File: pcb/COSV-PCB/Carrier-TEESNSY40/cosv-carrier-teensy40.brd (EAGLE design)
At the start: 96.8 x 26.7 mm, 21 parts, among them K1 61200821621, K2 61200821621, K3 61200821621

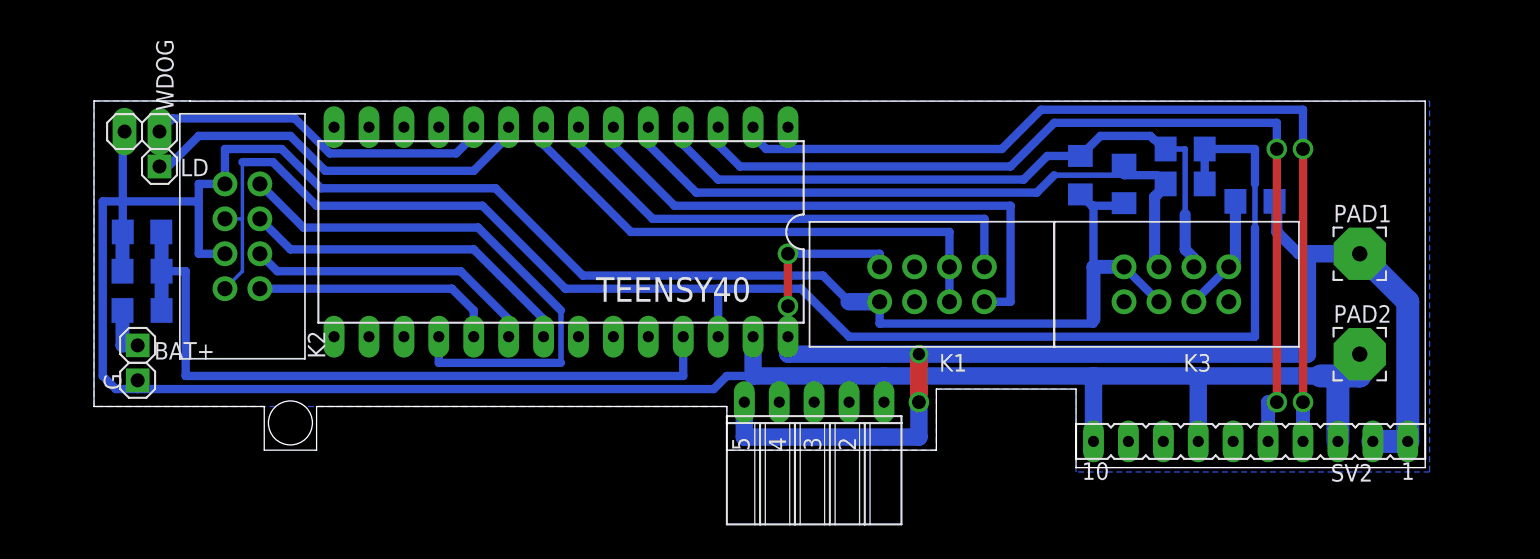
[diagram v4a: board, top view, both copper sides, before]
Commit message: Clean up part/pin names on board
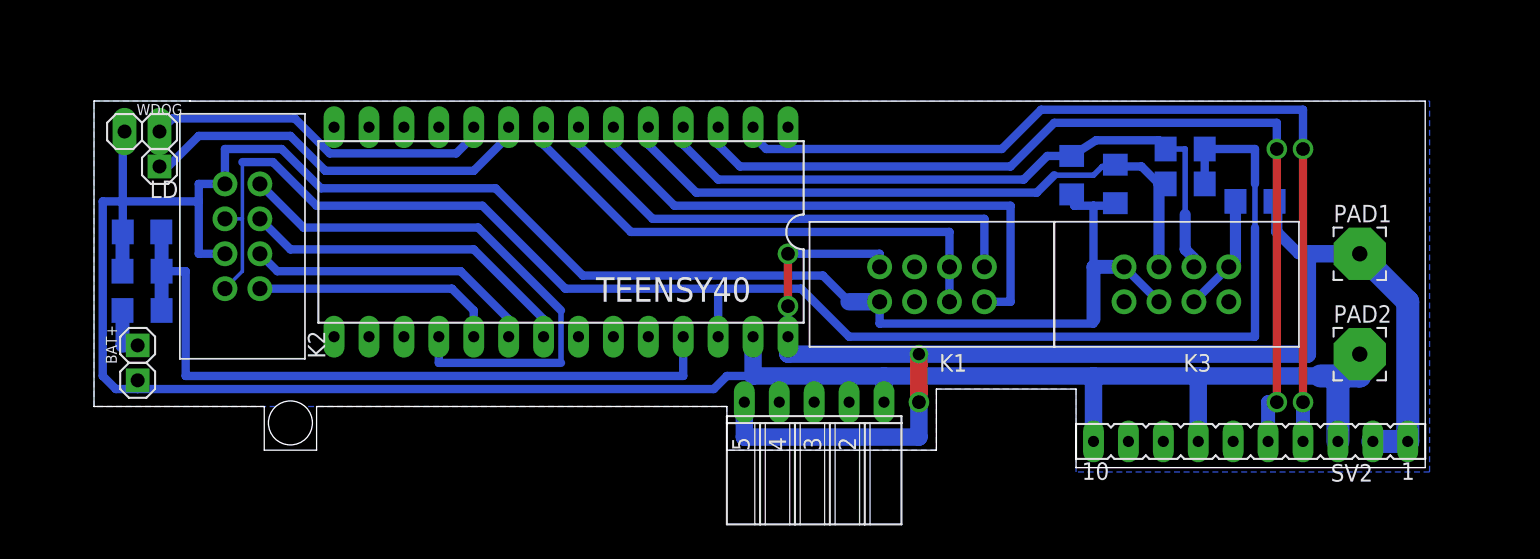
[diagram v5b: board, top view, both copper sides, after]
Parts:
- moved C2 0.64 mm to (74.6, 22.9)
- moved C3 0.64 mm to (77.8, 22.2)
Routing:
- net GND: track 242.4 -> 243.6 mm
- net ENCODER: track 48.4 -> 49.0 mm
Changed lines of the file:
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@@
 <?xml version="1.0" encoding="utf-8"?>
 <!DOCTYPE eagle SYSTEM "eagle.dtd">
-<eagle version="7.6.0">
+<eagle version="7.7.0">
 <drawing>
 <settings>
@@
 <text x="59.3725" y="16.8275" size="1.016" layer="27" rot="R180">vcc</text>
 <hole x="17.78" y="4.8387" drill="3.2"/>
+<text x="4.445" y="23.8125" size="1.016" layer="27">gnd</text>
+<text x="8.89" y="6.6675" size="1.016" layer="27" rot="R90">gnd</text>
 </plain>
 <attributes>
@@
 </element>
 <element name="BAT+" library="pinhead-2" package="1X01-S" value="" x="6.6675" y="10.4775" smashed="yes" rot="R270">
-<attribute name="NAME" x="7.8613" y="9.4488" size="1.27" layer="25" ratio="10"/>
+<attribute name="NAME" x="5.1562" y="9.1313" size="0.8128" layer="25" ratio="10" rot="R90"/>
 <attribute name="VALUE" x="3.4925" y="11.7475" size="1.27" layer="27" rot="R270"/>
 </element>
 <element name="GOLD_ORB_SM1" library="oshw" package="OSHW_8MM" value="OSHWLOGOLOGO8MM" x="27.305" y="19.05" rot="MR90"/>
 <element name="R3" library="resistor" package="R1206" value="2k2" x="82.8675" y="22.225" smashed="yes" rot="MR180">
-<attribute name="VALUE" x="86.36" y="23.495" size="1.27" layer="28" rot="MR270"/>
+<attribute name="VALUE" x="80.645" y="21.2725" size="1.27" layer="28" rot="MR180"/>
 </element>
 <element name="R4" library="resistor" package="R1206" value="2k2" x="82.8675" y="24.765" smashed="yes" rot="MR180">
-<attribute name="VALUE" x="86.36" y="26.035" size="1.27" layer="28" rot="MR270"/>
+<attribute name="VALUE" x="85.09" y="25.7175" size="1.27" layer="28" rot="MR0"/>
 </element>
 <element name="WDOG" library="pinhead" package="1X02" value="" x="6.985" y="26.035" smashed="yes">
-<attribute name="NAME" x="9.2837" y="27.5463" size="1.27" layer="25" ratio="10" rot="R90"/>
+<attribute name="NAME" x="6.5913" y="27.2288" size="0.8128" layer="25" ratio="10"/>
 <attribute name="VALUE" x="4.445" y="22.86" size="1.27" layer="27"/>
 </element>
 <element name="G" library="pinhead-2" package="1X01-S" value="" x="6.6675" y="7.9375" smashed="yes">
-<attribute name="NAME" x="5.4737" y="7.2263" size="1.27" layer="25" ratio="10" rot="R90"/>
 <attribute name="VALUE" x="5.3975" y="4.7625" size="1.27" layer="27"/>
 </element>
 <element name="LD" library="pinhead-2" package="1X01-S" value="" x="8.255" y="23.495" smashed="yes">
-<attribute name="NAME" x="9.7663" y="22.7838" size="1.27" layer="25" ratio="10"/>
+<attribute name="NAME" x="7.5438" y="21.1963" size="1.27" layer="25" ratio="10"/>
 <attribute name="VALUE" x="6.985" y="20.32" size="1.27" layer="27"/>
 </element>
-<element name="C2" library="rcl" package="C1206" value="10nf" x="75.2475" y="22.86" smashed="yes" rot="MR270">
-<attribute name="VALUE" x="76.2" y="20.32" size="1.27" layer="28" rot="MR270"/>
-</element>
-<element name="C3" library="rcl" package="C1206" value="10nf" x="78.4225" y="22.225" smashed="yes" rot="MR270">
-<attribute name="VALUE" x="79.375" y="19.685" size="1.27" layer="28" rot="MR270"/>
+<element name="C2" library="rcl" package="C1206" value="10nf" x="74.6125" y="22.86" smashed="yes" rot="MR270">
+<attribute name="VALUE" x="73.66" y="25.0825" size="1.27" layer="28" rot="MR270"/>
+</element>
+<element name="C3" library="rcl" package="C1206" value="10nf" x="77.7875" y="22.225" smashed="yes" rot="MR270">
+<attribute name="VALUE" x="78.74" y="20.0025" size="1.27" layer="28" rot="MR90"/>
 </element>
 <element name="K1" library="Wuerth_Elektronik_eiCan_05_Box_Header_IDC_Connectors_1_2" package="61200821621" value="61200821621" x="65.7225" y="14.9225" smashed="yes" rot="R180">
@@
 <contactref element="C3" pad="2"/>
 <wire x1="76.2" y1="20.6375" x2="76.2" y2="16.1925" width="0.6096" layer="16"/>
-<wire x1="75.2475" y1="21.46" x2="76.07" y2="20.6375" width="0.6096" layer="16"/>
-<wire x1="76.07" y1="20.6375" x2="76.2" y2="20.6375" width="0.6096" layer="16"/>
-<wire x1="78.4225" y1="20.825" x2="78.235" y2="20.6375" width="0.6096" layer="16"/>
+<wire x1="74.6125" y1="21.46" x2="74.8" y2="20.6375" width="0.6096" layer="16"/>
+<wire x1="74.8" y1="20.6375" x2="76.2" y2="20.6375" width="0.6096" layer="16"/>
+<wire x1="77.7875" y1="20.825" x2="78.235" y2="20.6375" width="0.6096" layer="16"/>
 <wire x1="78.235" y1="20.6375" x2="76.2" y2="20.6375" width="0.6096" layer="16"/>
 <contactref element="K3" pad="6"/>
@@
 <wire x1="48.895" y1="22.5425" x2="71.12" y2="22.5425" width="0.6096" layer="16"/>
 <wire x1="71.12" y1="22.5425" x2="72.8375" y2="24.26" width="0.6096" layer="16"/>
-<wire x1="72.8375" y1="24.26" x2="75.2475" y2="24.26" width="0.6096" layer="16"/>
-<wire x1="75.2475" y1="24.26" x2="76.705" y2="25.7175" width="0.6096" layer="16"/>
-<wire x1="76.705" y1="25.7175" x2="80.3275" y2="25.7175" width="0.6096" layer="16"/>
-<wire x1="80.3275" y1="25.7175" x2="80.493" y2="25.552" width="0.6096" layer="16"/>
-<wire x1="80.493" y1="25.552" x2="81.4455" y2="24.765" width="0.6096" layer="16"/>
+<wire x1="72.8375" y1="24.26" x2="74.6125" y2="24.26" width="0.6096" layer="16"/>
+<wire x1="74.6125" y1="24.26" x2="76.3875" y2="25.4" width="0.6096" layer="16"/>
+<wire x1="76.3875" y1="25.4" x2="80.9625" y2="25.4" width="0.6096" layer="16"/>
 <wire x1="83.5025" y1="16.1925" x2="83.5025" y2="16.8275" width="0.8128" layer="16"/>
 <wire x1="83.5025" y1="16.8275" x2="82.8675" y2="17.4625" width="0.8128" layer="16"/>
 <wire x1="82.8675" y1="17.4625" x2="82.8675" y2="20.0025" width="0.8128" layer="16"/>
 <wire x1="82.8675" y1="24.765" x2="82.8675" y2="20.0025" width="0.4064" layer="16"/>
-<wire x1="82.8675" y1="24.765" x2="81.4455" y2="24.765" width="0.4064" layer="16"/>
+<wire x1="82.8675" y1="24.765" x2="81.5975" y2="24.765" width="0.4064" layer="16"/>
+<wire x1="80.9625" y1="25.4" x2="81.5975" y2="24.765" width="0.6096" layer="16"/>
+<wire x1="81.5975" y1="24.765" x2="81.4455" y2="24.765" width="0.6096" layer="16"/>
 </signal>
 <signal name="ENCODER">
@@
 <contactref element="R3" pad="1"/>
 <wire x1="72.0725" y1="21.59" x2="73.3425" y2="22.86" width="0.6096" layer="16"/>
-<wire x1="81.4455" y1="22.225" x2="80.8105" y2="22.86" width="0.6096" layer="16"/>
-<wire x1="80.8105" y1="22.86" x2="78.4225" y2="22.86" width="0.6096" layer="16"/>
-<wire x1="78.4225" y1="22.86" x2="73.3425" y2="22.86" width="0.4064" layer="16"/>
-<wire x1="78.4225" y1="23.625" x2="78.4225" y2="22.86" width="0.6096" layer="16"/>
-<wire x1="80.9625" y1="16.1925" x2="80.645" y2="16.51" width="0.8128" layer="16"/>
-<wire x1="80.645" y1="16.51" x2="80.645" y2="21.2725" width="0.8128" layer="16"/>
-<wire x1="80.645" y1="21.2725" x2="81.4455" y2="22.073" width="0.8128" layer="16"/>
+<wire x1="81.4455" y1="22.225" x2="80.9625" y2="22.225" width="0.6096" layer="16"/>
+<wire x1="80.9625" y1="22.225" x2="79.6925" y2="23.495" width="0.6096" layer="16"/>
+<wire x1="79.6925" y1="23.495" x2="78.4225" y2="23.495" width="0.6096" layer="16"/>
+<wire x1="78.4225" y1="23.495" x2="76.835" y2="23.495" width="0.4064" layer="16"/>
+<wire x1="76.835" y1="23.495" x2="76.2" y2="22.86" width="0.4064" layer="16"/>
+<wire x1="76.2" y1="22.86" x2="73.3425" y2="22.86" width="0.4064" layer="16"/>
+<wire x1="77.7875" y1="23.625" x2="78.4225" y2="23.495" width="0.6096" layer="16"/>
+<wire x1="80.9625" y1="16.1925" x2="80.9625" y2="22.225" width="0.8128" layer="16"/>
+<wire x1="80.9625" y1="22.225" x2="81.4455" y2="22.073" width="0.8128" layer="16"/>
 <wire x1="81.4455" y1="22.073" x2="81.4455" y2="22.225" width="0.8128" layer="16"/>
 </signal>

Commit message: Update millable COSV carrier PCB to support milling with a dremel spindle This adds a few more jumpers, but it eliminates the tiny traces between pins that plague milling a board with a dremel spindle.
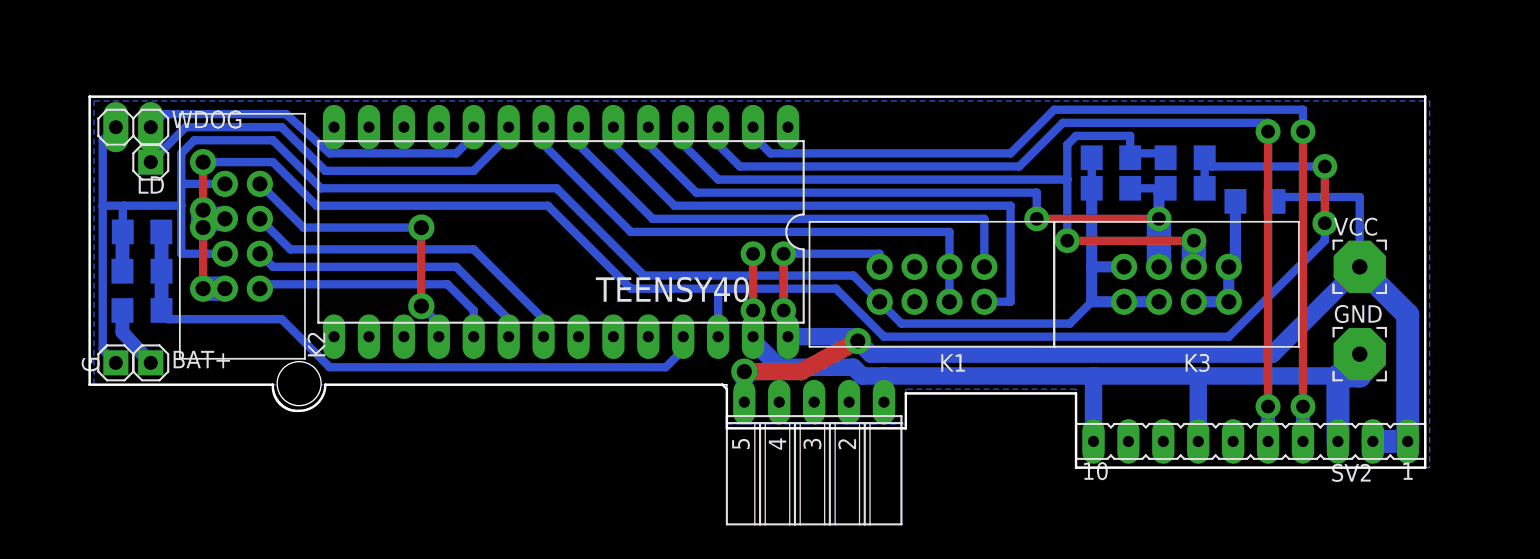
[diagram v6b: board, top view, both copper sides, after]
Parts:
- removed PAD1: WIREPAD3,81/1,1, wirepad:3,81/1,1
- added VCC: WIREPAD3,81/1,1, wirepad:3,81/1,1
- moved C2 3.13 mm to (77.5, 24.1), turned to 0 degrees
- moved G 2.03 mm to (5.08, 9.21)
- moved BAT+ 1.59 mm to (7.62, 9.21)
- moved LD 0.71 mm to (7.62, 23.8)
- moved WDOG 0.71 mm to (6.35, 26.4)
- moved R4 0.64 mm to (82.9, 24.1)
- moved C3 0.45 mm to (77.5, 21.9), turned to 0 degrees
- moved R3 0.32 mm to (82.9, 21.9)
- renumbered PAD2 to GND
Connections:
- net GND: now also K3.8
- net N$1: now also K3.2
- net VCC: now also VCC.1; no longer PAD1.1
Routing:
- net GND: track 243.6 -> 203.9 mm, vias 0 -> 2
- net SCL1: track 40.3 -> 21.5 mm, vias 0 -> 2
- net VCC: track 107.9 -> 98.2 mm
- net 3V3: track 113.3 -> 122.3 mm, vias 0 -> 6
- net HOME: track 49.1 -> 57.7 mm, vias 0 -> 2
- net A_BATTERY: track 54.6 -> 47.3 mm
- net ENCODER: track 49.0 -> 50.9 mm, vias 0 -> 2
- net N$1: track 8.55 -> 10.0 mm
- net TX1: track 67.7 -> 66.4 mm
- net LINE_DETECT: track 29.1 -> 30.1 mm
- net BAT+: track 3.64 -> 4.62 mm
- net PULSER: track 25.5 -> 26.1 mm
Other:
- board size 96.8 x 26.7 mm -> 97.2 x 27 mm
